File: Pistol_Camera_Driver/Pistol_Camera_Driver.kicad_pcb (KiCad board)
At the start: 2 copper layers, 95.8 x 46.1 mm, 68 parts, among them J1 Screw_Terminal_01x02, J10 Bluetooth, J11 Screw_Terminal_01x02, J12 Screw_Terminal_01x02, J13 I2C, J2 Objective, J3 Screw_Terminal_01x02, J4 Screw_Terminal_01x02, J6 Joystick, J7 Screw_Terminal_01x02, J9 Screw_Terminal_01x02, K1 IM03, Q1 locked, U1 LM7805_TO220, U10 RS0101YH6, U11 LDD-700L, U12 RS0101YH6, U13 LDD-700L, U2 LM317_TO-263, U3 Raspberri_Pi_Pico, U4 DRV8834PWP, U5 DRV8834PWP, U6 RS0101YH6, U7 LDD-700L, U8 RS0101YH6, U9 LDD-700L

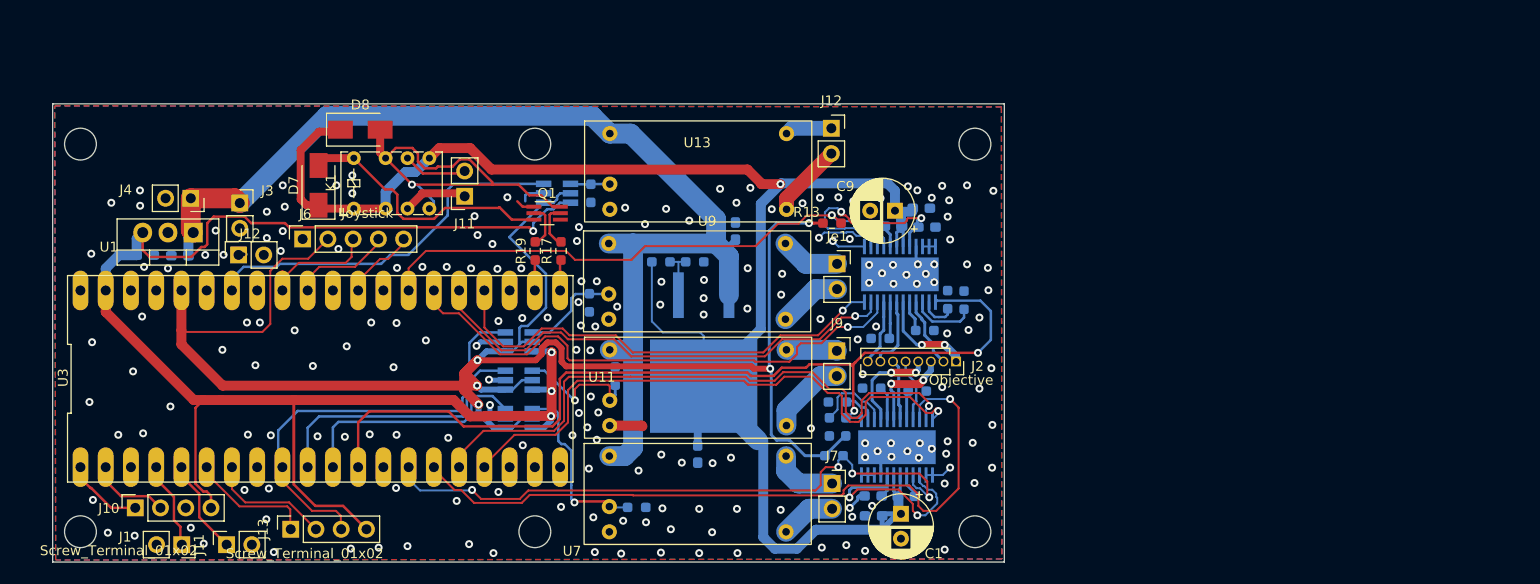
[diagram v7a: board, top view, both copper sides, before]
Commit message: v2.5 ready without end stoppers
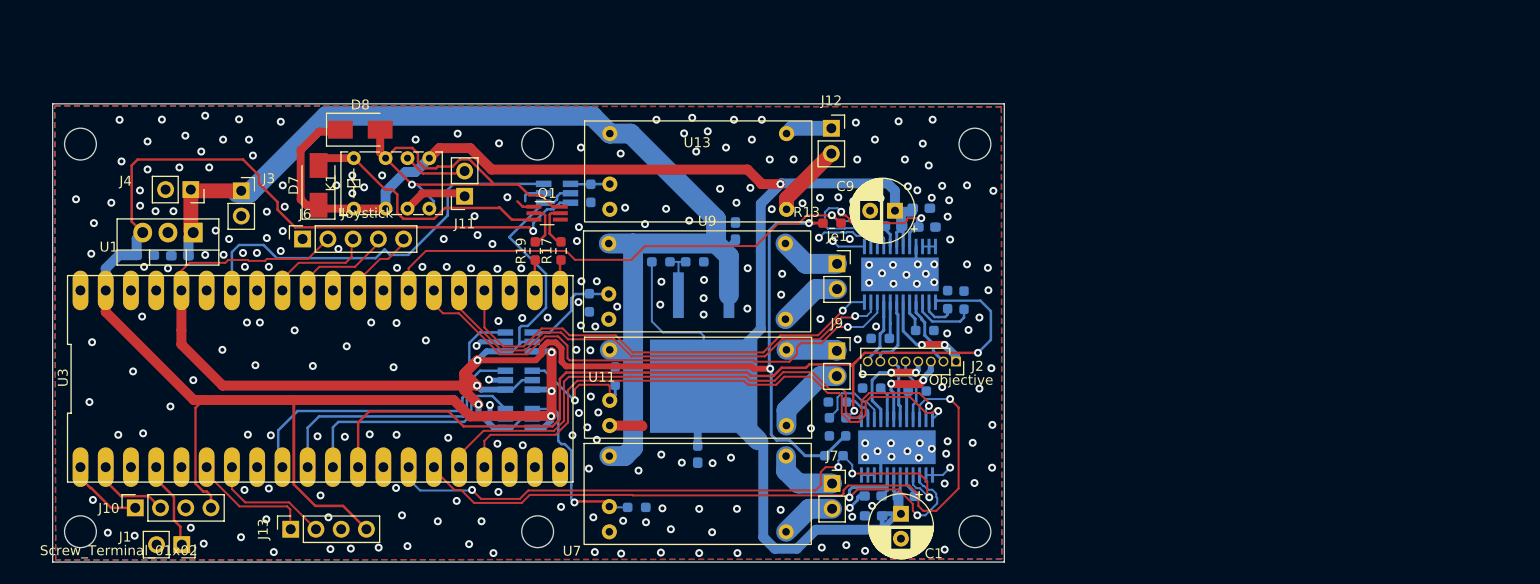
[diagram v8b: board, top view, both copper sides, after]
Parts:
- removed the J11 at (42.4, 76.0)
- removed the J12 at (43.5, 46.8)
- moved J3 1.24 mm to (43.8, 40.4)
- moved J4 0.88 mm to (38.8, 40.2)
- moved REF** 0.28 mm to (73.6, 74.7)
- moved REF** 0.28 mm to (73.6, 35.6)
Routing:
- net unconnected-(U3-Pad5): track 9.68 -> 0.89 mm
- net PWM_WHITE: track 47.2 -> 38.7 mm
- net +5V: track 153.7 -> 160.6 mm
- net +3V3: track 177.3 -> 173.9 mm
- net PWM_IR: track 39.1 -> 42.3 mm
- net DIR1: track 58.6 -> 60.0 mm
- net +12V: track 113.9 -> 114.6 mm
- net GND: vias 201 -> 260
